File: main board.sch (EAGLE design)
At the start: 62 parts, among them SW1 BOOT_SW, SW2 RST_SW, X1 MINI-USB, Y1 SMDRESONATOR

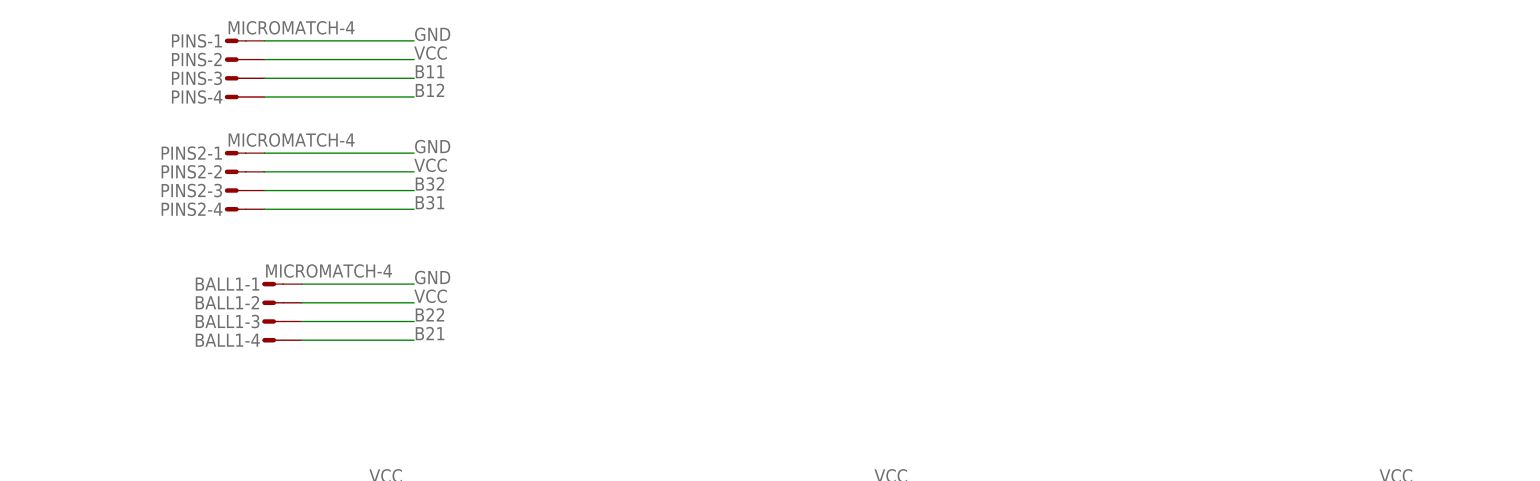
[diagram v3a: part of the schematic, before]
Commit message: Also added some caps for button or whatever ports.
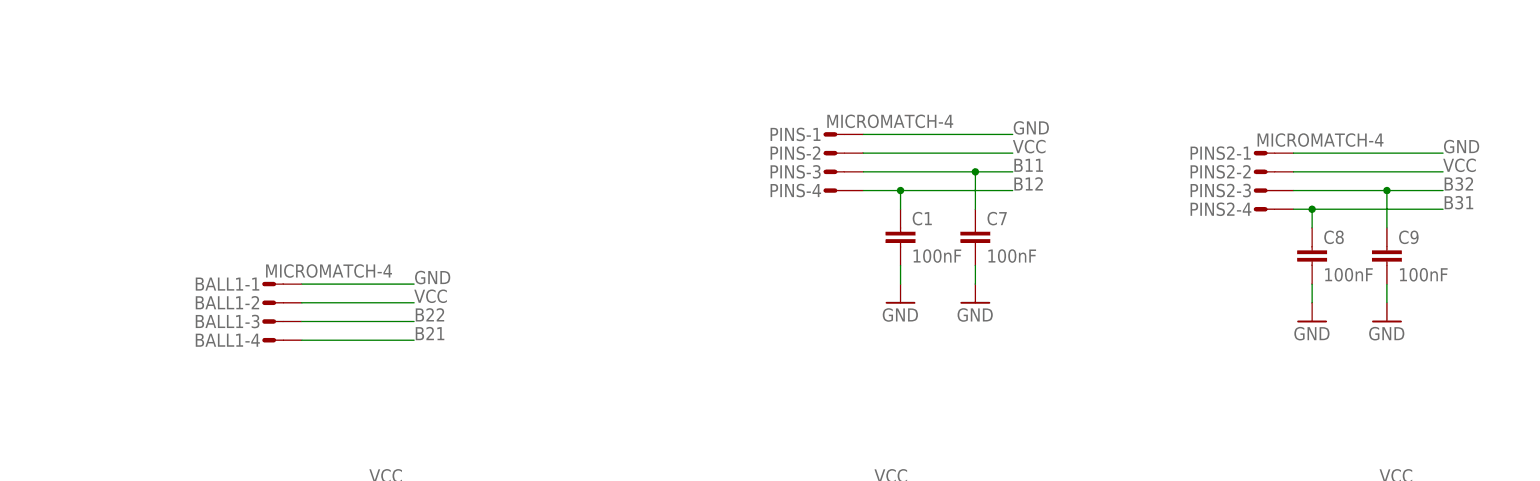
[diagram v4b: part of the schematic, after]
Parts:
- added C1, C7, C8, C9: 100nF, rcl:C-EUC0603
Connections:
- net B11: now also C7.1
- net B12: now also C1.1
- net B31: now also C8.1
- net B32: now also C9.1
- net GND: now also C1.2, C7.2, C8.2, C9.2
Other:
- moved on the sheet: PINS-1, PINS-2, PINS-3, PINS-4, PINS2-1, PINS2-2, PINS2-3, PINS2-4
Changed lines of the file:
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@@
 <part name="PINS" library="con-amp-micromatch" deviceset="MICROMATCH-4" device=""/>
 <part name="R4" library="rcl" deviceset="R-EU_" device="R0603" value="120"/>
+<part name="C1" library="rcl" deviceset="C-EU" device="C0603" value="100nF"/>
+<part name="C7" library="rcl" deviceset="C-EU" device="C0603" value="100nF"/>
+<part name="GND31" library="supply1" deviceset="GND" device=""/>
+<part name="GND32" library="supply1" deviceset="GND" device=""/>
+<part name="C8" library="rcl" deviceset="C-EU" device="C0603" value="100nF"/>
+<part name="C9" library="rcl" deviceset="C-EU" device="C0603" value="100nF"/>
+<part name="GND33" library="supply1" deviceset="GND" device=""/>
+<part name="GND34" library="supply1" deviceset="GND" device=""/>
 </parts>
 <sheets>
@@
 <instance part="485" gate="-3" x="63.5" y="91.44"/>
 <instance part="485" gate="-4" x="63.5" y="88.9"/>
-<instance part="PINS2" gate="-1" x="190.5" y="121.92"/>
-<instance part="PINS2" gate="-2" x="190.5" y="119.38"/>
-<instance part="PINS2" gate="-3" x="190.5" y="116.84"/>
-<instance part="PINS2" gate="-4" x="190.5" y="114.3"/>
-<instance part="PINS" gate="-1" x="190.5" y="137.16"/>
-<instance part="PINS" gate="-2" x="190.5" y="134.62"/>
-<instance part="PINS" gate="-3" x="190.5" y="132.08"/>
-<instance part="PINS" gate="-4" x="190.5" y="129.54"/>
+<instance part="PINS2" gate="-1" x="330.2" y="121.92"/>
+<instance part="PINS2" gate="-2" x="330.2" y="119.38"/>
+<instance part="PINS2" gate="-3" x="330.2" y="116.84"/>
+<instance part="PINS2" gate="-4" x="330.2" y="114.3"/>
+<instance part="PINS" gate="-1" x="271.78" y="124.46"/>
+<instance part="PINS" gate="-2" x="271.78" y="121.92"/>
+<instance part="PINS" gate="-3" x="271.78" y="119.38"/>
+<instance part="PINS" gate="-4" x="271.78" y="116.84"/>
 <instance part="R4" gate="G$1" x="96.52" y="121.92" rot="R90"/>
+<instance part="C1" gate="G$1" x="281.94" y="111.76"/>
+<instance part="C7" gate="G$1" x="292.1" y="111.76"/>
+<instance part="GND31" gate="1" x="281.94" y="101.6"/>
+<instance part="GND32" gate="1" x="292.1" y="101.6"/>
+<instance part="C8" gate="G$1" x="337.82" y="109.22"/>
+<instance part="C9" gate="G$1" x="347.98" y="109.22"/>
+<instance part="GND33" gate="1" x="337.82" y="99.06"/>
+<instance part="GND34" gate="1" x="347.98" y="99.06"/>
 </instances>
 <busses>
@@
 <segment>
 <pinref part="PINS" gate="-1" pin="S"/>
-<wire x1="195.58" y1="137.16" x2="215.9" y2="137.16" width="0.1524" layer="91"/>
-<label x="215.9" y="137.16" size="1.778" layer="95"/>
+<wire x1="276.86" y1="124.46" x2="297.18" y2="124.46" width="0.1524" layer="91"/>
+<label x="297.18" y="124.46" size="1.778" layer="95"/>
 </segment>
 <segment>
 <pinref part="PINS2" gate="-1" pin="S"/>
-<wire x1="195.58" y1="121.92" x2="215.9" y2="121.92" width="0.1524" layer="91"/>
-<label x="215.9" y="121.92" size="1.778" layer="95"/>
+<wire x1="335.28" y1="121.92" x2="355.6" y2="121.92" width="0.1524" layer="91"/>
+<label x="355.6" y="121.92" size="1.778" layer="95"/>
+</segment>
+<segment>
+<pinref part="C1" gate="G$1" pin="2"/>
+<wire x1="281.94" y1="106.68" x2="281.94" y2="104.14" width="0.1524" layer="91"/>
+<pinref part="GND31" gate="1" pin="GND"/>
+</segment>
+<segment>
+<pinref part="C7" gate="G$1" pin="2"/>
+<wire x1="292.1" y1="106.68" x2="292.1" y2="104.14" width="0.1524" layer="91"/>
+<pinref part="GND32" gate="1" pin="GND"/>
+</segment>
+<segment>
+<pinref part="C8" gate="G$1" pin="2"/>
+<wire x1="337.82" y1="104.14" x2="337.82" y2="101.6" width="0.1524" layer="91"/>
+<pinref part="GND33" gate="1" pin="GND"/>
+</segment>
+<segment>
+<pinref part="C9" gate="G$1" pin="2"/>
+<wire x1="347.98" y1="104.14" x2="347.98" y2="101.6" width="0.1524" layer="91"/>
+<pinref part="GND34" gate="1" pin="GND"/>
 </segment>
 </net>
@@
 <segment>
 <pinref part="PINS" gate="-2" pin="S"/>
-<wire x1="195.58" y1="134.62" x2="215.9" y2="134.62" width="0.1524" layer="91"/>
-<label x="215.9" y="134.62" size="1.778" layer="95"/>
+<wire x1="276.86" y1="121.92" x2="297.18" y2="121.92" width="0.1524" layer="91"/>
+<label x="297.18" y="121.92" size="1.778" layer="95"/>
 </segment>
 <segment>
 <pinref part="PINS2" gate="-2" pin="S"/>
-<wire x1="195.58" y1="119.38" x2="215.9" y2="119.38" width="0.1524" layer="91"/>
-<label x="215.9" y="119.38" size="1.778" layer="95"/>
+<wire x1="335.28" y1="119.38" x2="355.6" y2="119.38" width="0.1524" layer="91"/>
+<label x="355.6" y="119.38" size="1.778" layer="95"/>
 </segment>
 </net>
@@
 <segment>
 <pinref part="PINS" gate="-3" pin="S"/>
-<wire x1="195.58" y1="132.08" x2="215.9" y2="132.08" width="0.1524" layer="91"/>
-<label x="215.9" y="132.08" size="1.778" layer="95"/>
+<wire x1="276.86" y1="119.38" x2="292.1" y2="119.38" width="0.1524" layer="91"/>
+<label x="297.18" y="119.38" size="1.778" layer="95"/>
+<pinref part="C7" gate="G$1" pin="1"/>
+<wire x1="292.1" y1="119.38" x2="297.18" y2="119.38" width="0.1524" layer="91"/>
+<wire x1="292.1" y1="114.3" x2="292.1" y2="119.38" width="0.1524" layer="91"/>
+<junction x="292.1" y="119.38"/>
 </segment>
 </net>
@@
 <segment>
 <pinref part="PINS" gate="-4" pin="S"/>
-<wire x1="195.58" y1="129.54" x2="215.9" y2="129.54" width="0.1524" layer="91"/>
-<label x="215.9" y="129.54" size="1.778" layer="95"/>
+<wire x1="276.86" y1="116.84" x2="281.94" y2="116.84" width="0.1524" layer="91"/>
+<label x="297.18" y="116.84" size="1.778" layer="95"/>
+<pinref part="C1" gate="G$1" pin="1"/>
+<wire x1="281.94" y1="116.84" x2="297.18" y2="116.84" width="0.1524" layer="91"/>
+<wire x1="281.94" y1="114.3" x2="281.94" y2="116.84" width="0.1524" layer="91"/>
+<junction x="281.94" y="116.84"/>
 </segment>
 </net>
@@
 <segment>
 <pinref part="PINS2" gate="-3" pin="S"/>
-<wire x1="195.58" y1="116.84" x2="215.9" y2="116.84" width="0.1524" layer="91"/>
-<label x="215.9" y="116.84" size="1.778" layer="95"/>
+<wire x1="335.28" y1="116.84" x2="347.98" y2="116.84" width="0.1524" layer="91"/>
+<label x="355.6" y="116.84" size="1.778" layer="95"/>
+<pinref part="C9" gate="G$1" pin="1"/>
+<wire x1="347.98" y1="116.84" x2="355.6" y2="116.84" width="0.1524" layer="91"/>
+<wire x1="347.98" y1="111.76" x2="347.98" y2="116.84" width="0.1524" layer="91"/>
+<junction x="347.98" y="116.84"/>
 </segment>
 </net>
@@
 <segment>
 <pinref part="PINS2" gate="-4" pin="S"/>
-<wire x1="195.58" y1="114.3" x2="215.9" y2="114.3" width="0.1524" layer="91"/>
-<label x="215.9" y="114.3" size="1.778" layer="95"/>
-</segment>
-</net>
+<wire x1="335.28" y1="114.3" x2="337.82" y2="114.3" width="0.1524" layer="91"/>
+<label x="355.6" y="114.3" size="1.778" layer="95"/>
+<pinref part="C8" gate="G$1" pin="1"/>
+<wire x1="337.82" y1="114.3" x2="355.6" y2="114.3" width="0.1524" layer="91"/>
+<wire x1="337.82" y1="111.76" x2="337.82" y2="114.3" width="0.1524" layer="91"/>
+<junction x="337.82" y="114.3"/>
+</segment>
+</net>
